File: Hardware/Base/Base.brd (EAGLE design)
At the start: 127 x 101.6 mm, 70 parts, among them IC1 74LS245N, T1 2N3904, T10 2N3904, T11 2N3904, T2 2N3904, T3 2N3904, T4 2N3904, T5 2N3904, T6 2N3904, T7 2N3904, T8 2N3904, T9 2N3904

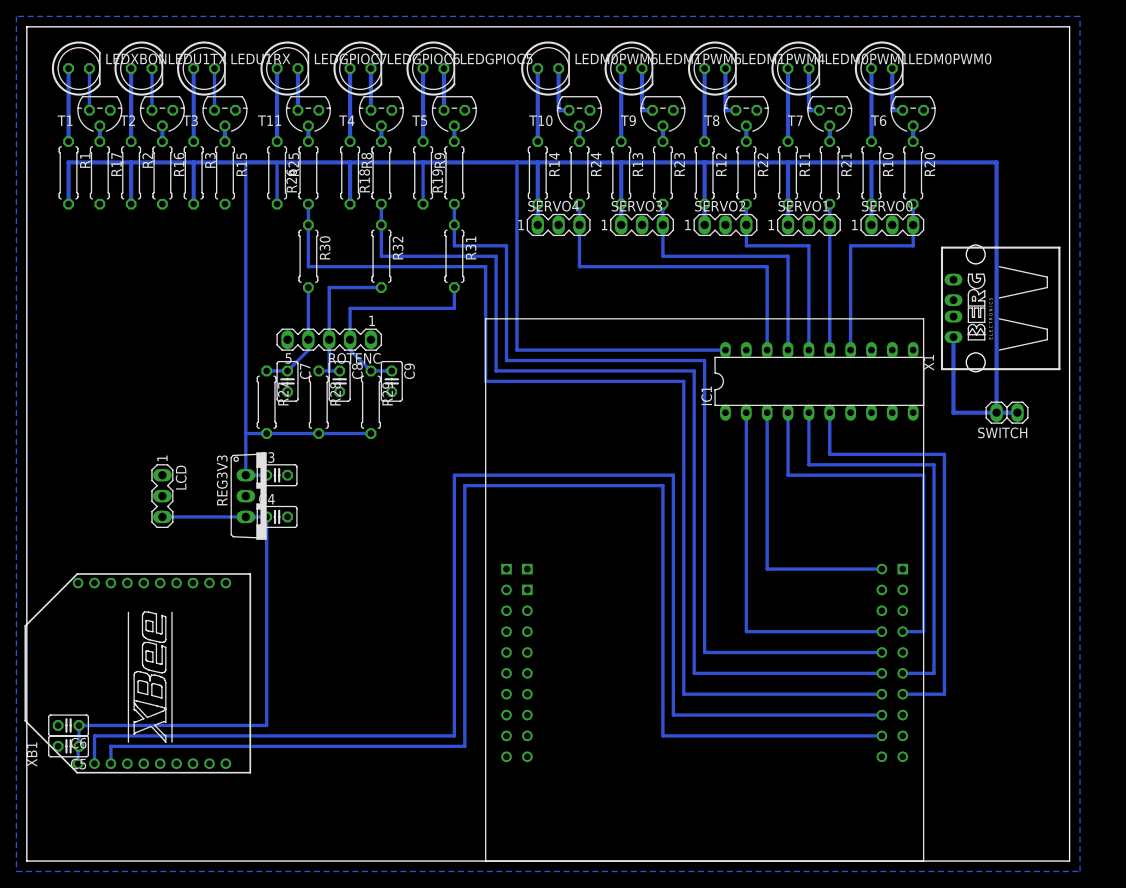
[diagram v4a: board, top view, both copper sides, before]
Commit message: No airwires.
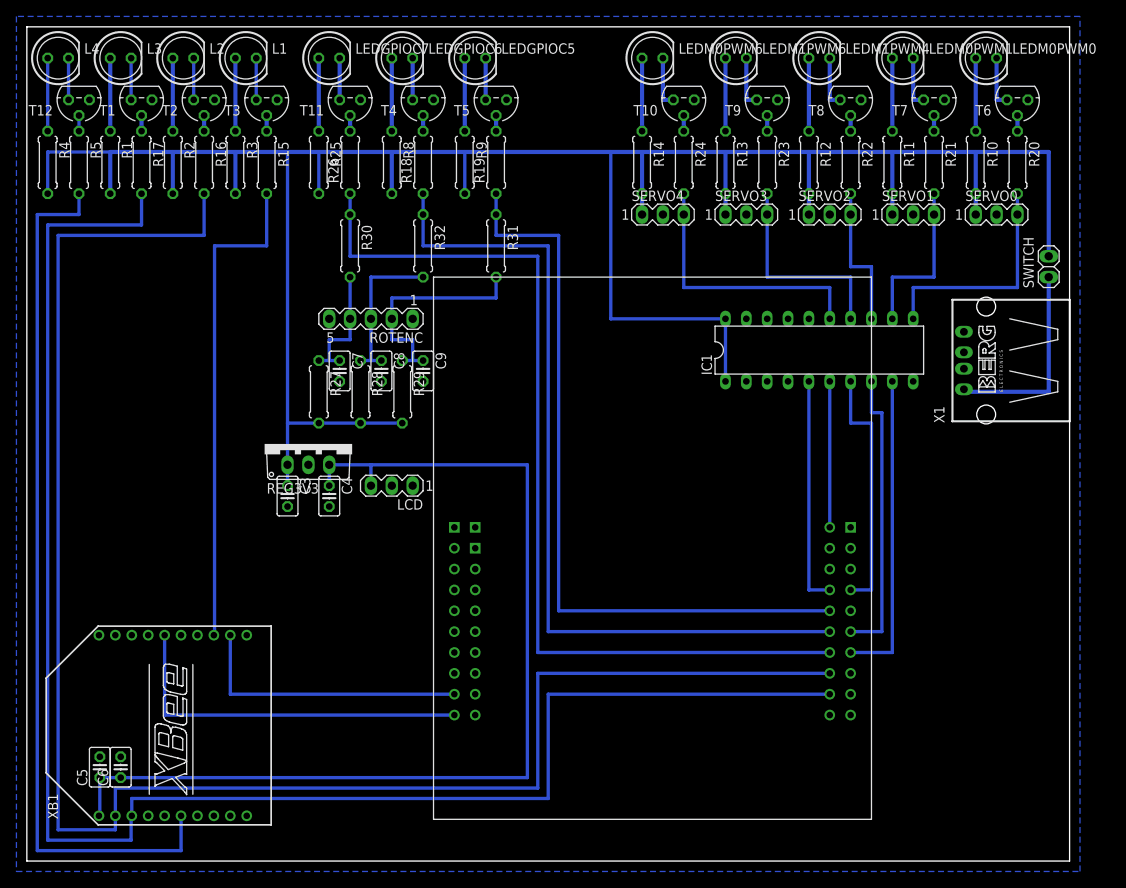
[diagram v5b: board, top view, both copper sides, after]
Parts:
- removed LEDU1RX, LEDU1TX, LEDXBON: (no value), led:LED5MM
- added L1, L2, L3, L4: (no value), led:LED5MM
- added R4, R5: (no value), rcl:0207/7
- added T12: 2N3904, transistor:TO92
- moved LCD 28.0 mm to (44.5, 45.7), turned to 180 degrees
- moved SWITCH 18.5 mm to (124.5, 72.4), turned to 90 degrees
- moved R14 12.8 mm to (74.9, 85.1)
- moved LEDM0PWM0 12.8 mm to (116.8, 97.8)
- moved LEDM0PWM1 12.8 mm to (106.7, 97.8)
- moved LEDM0PWM6 12.8 mm to (76.2, 97.8)
- moved LEDM1PWM4 12.8 mm to (96.5, 97.8)
- moved LEDM1PWM6 12.8 mm to (86.4, 97.8)
- moved R11 12.8 mm to (105.4, 85.1)
- moved R12 12.8 mm to (95.2, 85.1)
- moved R13 12.8 mm to (85.1, 85.1)
- moved R20 12.8 mm to (120.7, 85.1)
- moved R22 12.8 mm to (100.3, 85.1)
- moved R23 12.8 mm to (90.2, 85.1)
- moved R24 12.8 mm to (80.0, 85.1)
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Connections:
- new net N$43: L4.K, T12.1
- new net N$44: L4.A, R4.1
- new net N$45: R5.1, T12.2
- net 5V: now also IC1.1, R4.2
- net CTS: now also TIVA.PA6; no longer TIVA.PA5
- net GND: now also IC1.16, IC1.17, IC1.18, IC1.19, IC1.2, IC1.3, IC1.4, T12.3
- net M0PWM0: now also IC1.11; no longer IC1.14
- net M0PWM1: now also IC1.12; no longer IC1.15
- net M0PWM6: now also IC1.15; no longer IC1.18
- net M1PWM4: now also IC1.13; no longer IC1.16
- net M1PWM6: now also IC1.14; no longer IC1.17
- net N$1: now also L3.K; no longer LEDXBON.K
- net N$2: now also L2.K; no longer LEDU1TX.K
- net N$3: now also L2.A; no longer LEDU1TX.A
- net N$39: now also IC1.7; no longer IC1.4
- net N$4: now also L3.A; no longer LEDXBON.A
- net N$40: now also IC1.6; no longer IC1.3
- net N$41: now also IC1.8; no longer IC1.5
- net N$42: now also IC1.9; no longer IC1.6
- net N$5: now also L1.K; no longer LEDU1RX.K
- net N$6: now also L1.A; no longer LEDU1RX.A
- net N$8: now also IC1.5; no longer IC1.2
- net RSSI: now also R5.2; no longer TIVA.PA7
- net RTS: now also TIVA.PA7; no longer TIVA.PA6
- net U1RX: now also R16.2; no longer R15.2
- net U1TX: now also R17.2; no longer R16.2
- net XBON: now also R15.2; no longer R17.2
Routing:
- net RSSI: track 0.00 -> 106.8 mm
- net XBON: track 0.00 -> 60.2 mm
- net 3V3: track 65.8 -> 124.2 mm
- net U1RX: track 160.2 -> 208.3 mm
- net RTS: track 0.00 -> 45.0 mm
- net U1TX: track 158.2 -> 203.2 mm
- net CTS: track 0.00 -> 34.5 mm
- net GPIOC5: track 106.7 -> 91.4 mm
- net N$8: track 43.2 -> 27.9 mm
- net N$42: track 53.3 -> 38.1 mm
- net N$40: track 33.0 -> 17.8 mm
- net N$39: track 45.7 -> 30.5 mm
- net N$41: track 50.8 -> 35.6 mm
- net GPIOC7: track 129.5 -> 114.3 mm
- net GPIOC6: track 118.1 -> 102.9 mm
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
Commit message: First printable.
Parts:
- moved C6 27.4 mm to (38.1, 17.8)
- moved C5 26.2 mm to (34.3, 17.8)
- moved LCD 14.5 mm to (40.6, 31.8)
- moved R10 8.13 mm to (120.7, 91.4)
- moved R11 8.13 mm to (110.5, 91.4)
- moved R12 8.13 mm to (100.3, 91.4)
- moved R13 8.13 mm to (90.2, 91.4)
- moved R14 8.13 mm to (80.0, 91.4)
- moved R1 7.41 mm to (14.0, 91.4)
- moved R3 7.41 mm to (29.2, 91.4)
- moved R4 7.41 mm to (6.35, 91.4)
- moved R2 7.41 mm to (21.6, 91.4)
- moved R25 7.41 mm to (39.4, 91.4)
- moved R8 7.41 mm to (48.3, 91.4)
- moved R9 7.41 mm to (57.1, 91.4)
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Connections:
- net GPIOE5: now also TIVA.PE5
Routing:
- net 5V: track 308.6 -> 283.2 mm
- net U1RX: track 208.3 -> 194.3 mm
- net U1TX: track 203.2 -> 194.2 mm
- net CTS: track 34.5 -> 28.1 mm
- net RTS: track 45.0 -> 38.7 mm
- net N$6: track 8.89 -> 3.81 mm
- net N$44: track 8.89 -> 3.81 mm
- net N$4: track 8.89 -> 3.81 mm
- net N$34: track 8.89 -> 3.81 mm
- net N$3: track 8.89 -> 3.81 mm
- net N$22: track 8.89 -> 3.81 mm
- net N$20: track 8.89 -> 3.81 mm
- net N$18: track 8.89 -> 3.81 mm
- net N$16: track 8.89 -> 3.81 mm
- net N$14: track 8.89 -> 3.81 mm
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
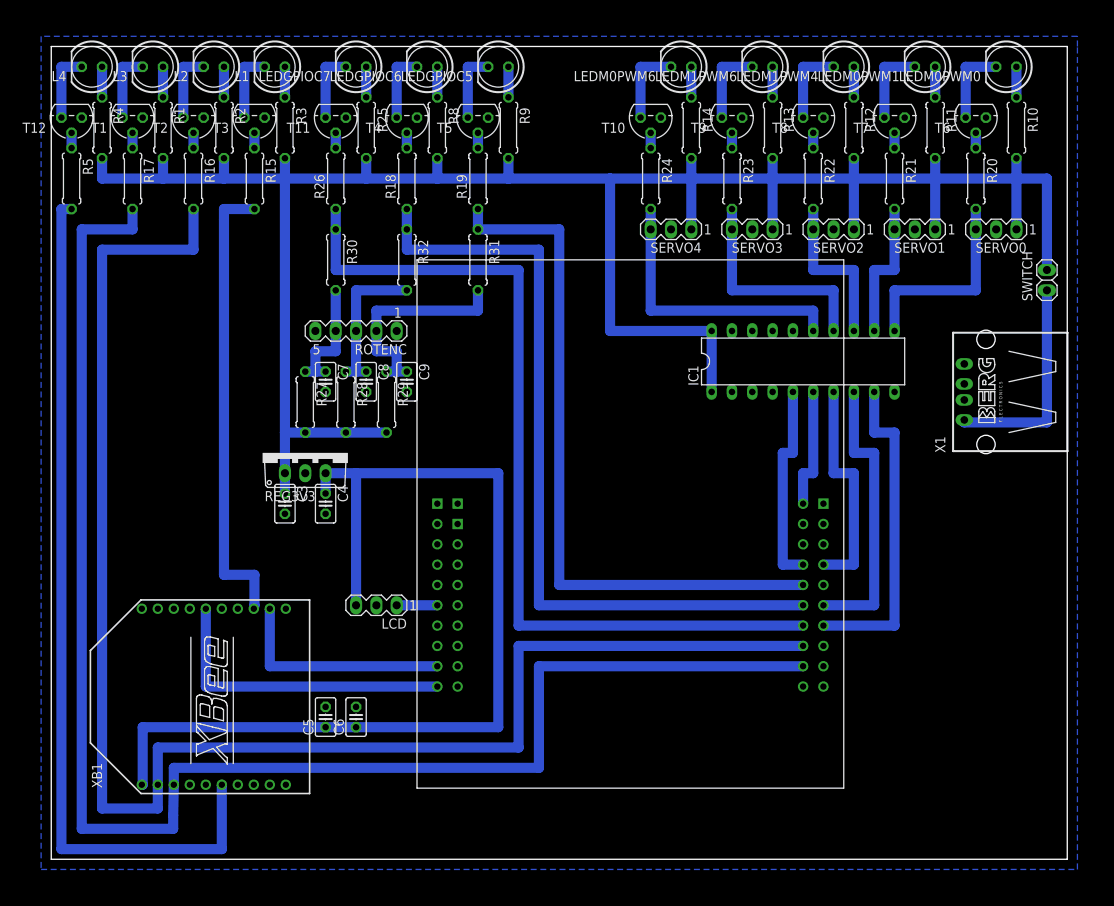
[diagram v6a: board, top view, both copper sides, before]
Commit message: Fixed Tiva dimensions.
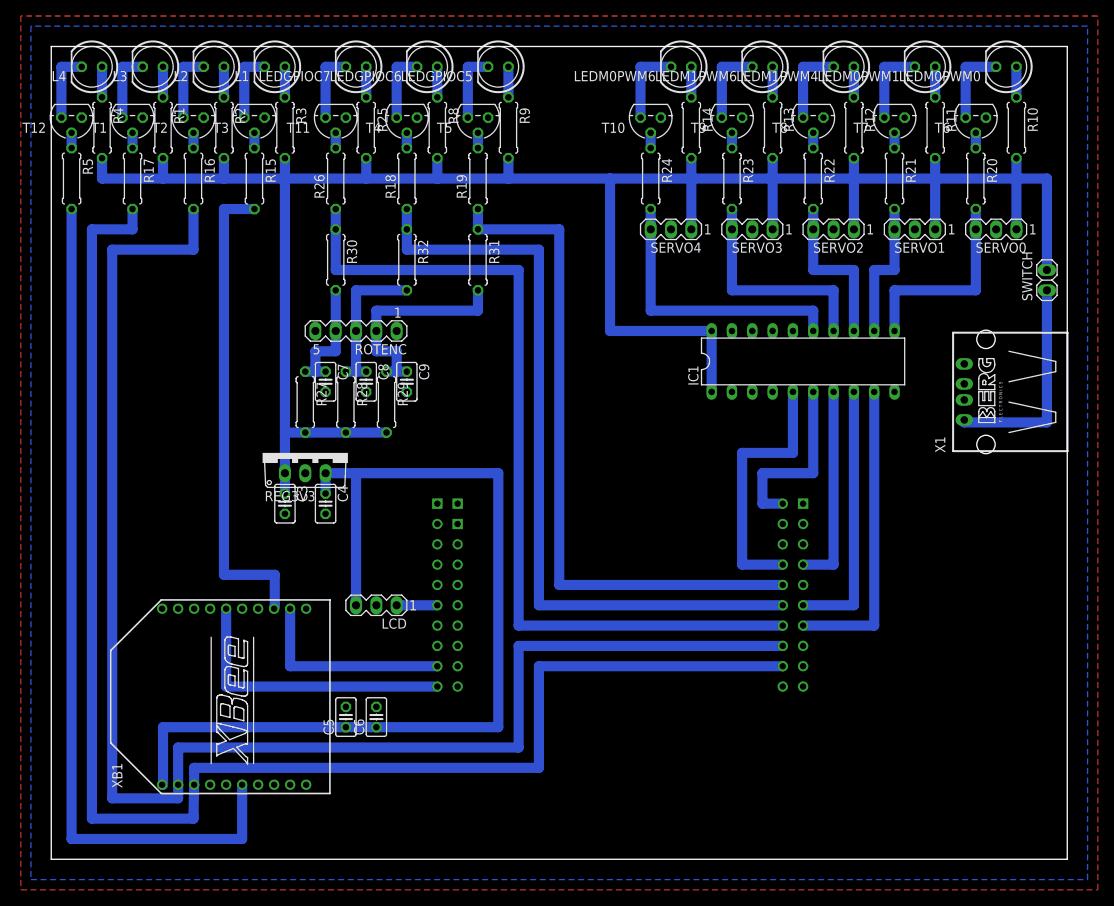
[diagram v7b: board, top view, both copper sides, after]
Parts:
- moved C5 2.54 mm to (36.8, 17.8)
- moved C6 2.54 mm to (40.6, 17.8)
- moved XB1 2.54 mm to (22.9, 20.3)
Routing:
- net U1TX: track 194.2 -> 186.6 mm
- net U1RX: track 194.3 -> 186.7 mm
- net N$8: track 25.4 -> 33.0 mm
- net N$40: track 15.2 -> 22.9 mm
- net N$41: track 35.6 -> 33.0 mm
- net GPIOC6: track 99.1 -> 96.5 mm
- net RTS: track 38.7 -> 36.1 mm
- net RSSI: track 109.4 -> 106.8 mm
- net GPIOC7: track 110.5 -> 108.0 mm
- net XBON: track 57.6 -> 60.1 mm
- net CTS: track 28.1 -> 25.6 mm
- net N$42: track 40.6 -> 38.1 mm
- net N$39: track 27.9 -> 25.4 mm
- net GPIOC5: track 87.6 -> 85.1 mm
- net 3V3: track 124.1 -> 121.6 mm
- added copper zone on layer 1, net GND

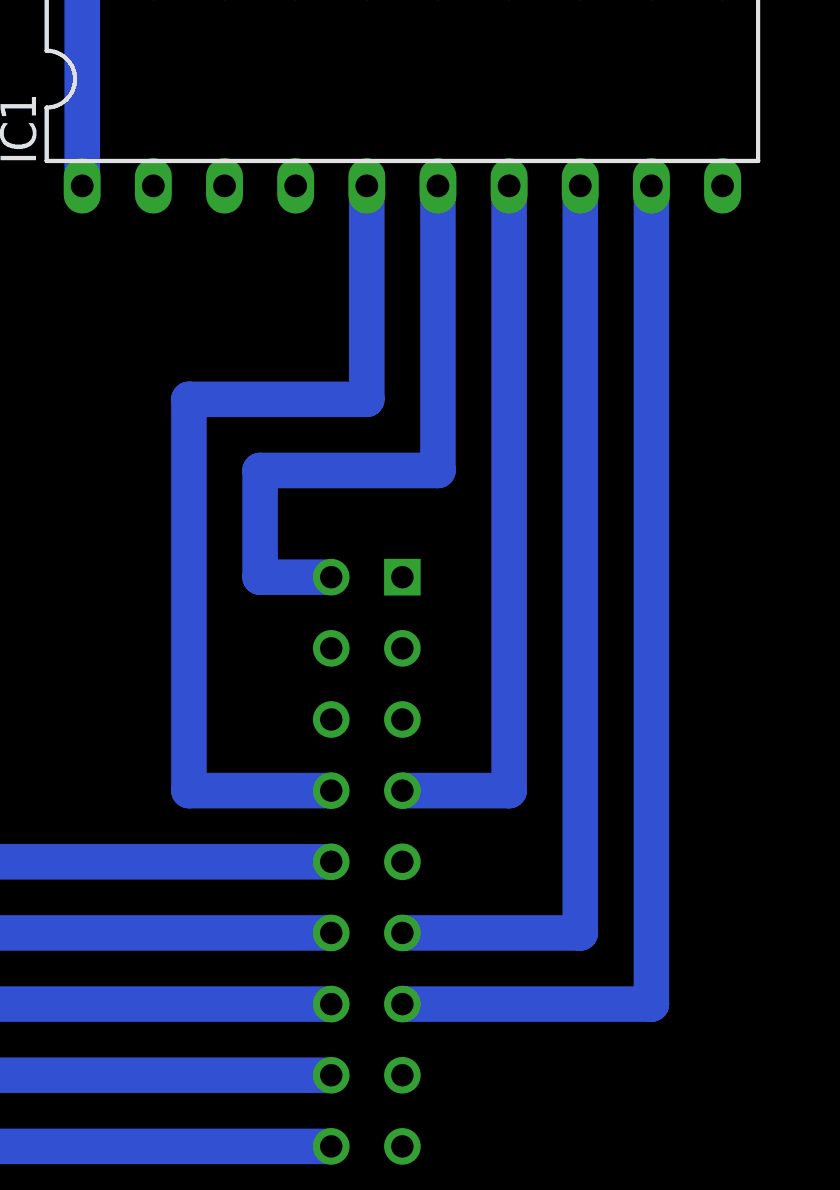
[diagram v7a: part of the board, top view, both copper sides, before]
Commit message: Wires prettied up in Base.brd/sch
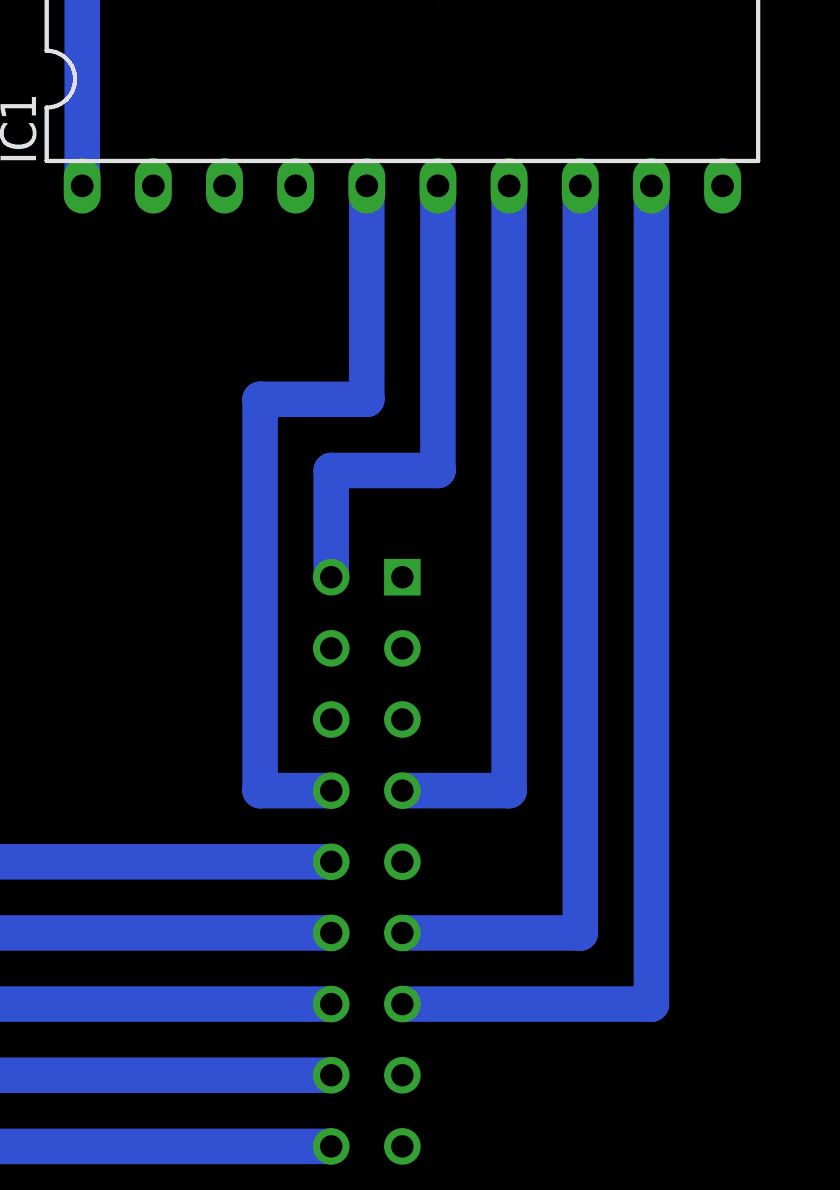
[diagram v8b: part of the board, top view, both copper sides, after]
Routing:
- net N$47: track 33.0 -> 27.9 mm
- net N$40: track 22.9 -> 17.8 mm
